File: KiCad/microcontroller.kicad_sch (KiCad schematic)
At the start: 48 parts, among them J4 Debugger, J5 STM32F051C6_male_header, SW1 Reset switch, SW2 switch, SW3 switch, SW4 switch, U7 24LC256

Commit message: Significant schematic changes
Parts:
- removed J5: STM32F051C6_male_header, symbol EEE3088F_CKR:STM32F051C6_male_header
- removed TP?: STM32 BOOT0, footprint:Testpoint_2.54mm, symbol Connector:TestPoint
- added J4: STM32F051C6_testpoints, symbol EEE3088F_CKR:STM32F051C6_testpoints
- added JP1, JP2, JP3, JP4, JP5, JP6: Jumper_2_Bridged, symbol Jumper:Jumper_2_Bridged
- added R48, R49, R50, R51, R57: 0, footprint:R0603, symbol Device:R
- renumbered J4 to J5, R52 to R34, R53 to R35, R30 to R36, R31 to R37, R32 to R38, R33 to R39, R34 to R40, R36 to R41, R37 to R42, R40 to R43, R41 to R44, R42 to R45, R43 to R46, R56 to R47, R61 to R60, R62 to R61, R63 to R62, R64 to R63
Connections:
- net INT_1 is gone; now on net INT: R?.1
- net uc29 is gone; now on net SW3: J3.29 (PA8_)
- net +3V3: now also J4.1 (_VBAT), J4.24 (_VDD), J4.48 (VDD_), J4.9 (_VDDA)
- net BOOT0: now also J4.44 (BOOT0_)
- net GND: now also J4.23 (_VSS), J4.47 (VSS_), J4.8 (_VSSA)
- net INT: now also J4.25 (PB12_)
- net LED1: now also J4.15 (_PA5)
- net LED2: now also J4.16 (_PA6)
- net Lght_P: now also J4.40 (PB4_)
- net NSRT: now also J4.7 (_NSRT)
- net POT: now also JP6.1 (A); no longer J3.19 (_PB1)
- net POT_P: now also J4.20 (_PB2)
- net Rx: now also J4.43 (PB7_)
- net SCL_1: now also JP1.1 (A); no longer J3.21 (_PB10), R?.1
- net SCL_2: now also JP3.1 (A); no longer J3.45 (PB8_), R?.1
- net SDA_1: now also JP2.1 (A); no longer J3.22 (_PB11), R?.1
- net SDA_2: now also JP4.1 (A); no longer J3.46 (PB9_), R?.1
- net SW1: now also J3.27 (PB14_), J4.27 (PB14_); no longer J3.26 (PB13_)
- net SW2: now also J3.28 (PB15_), J4.28 (PB15_); no longer J3.27 (PB14_)
- net SW3: now also J4.29 (PA8_); no longer J3.28 (PB15_)
- net SWCLK: now also J4.37 (PA14_)
- net SWDIO: now also J4.34 (PA13_)
- net THM: now also JP5.1 (A); no longer J3.18 (_PB0)
- net THM_P: now also J4.39 (PB3_)
- net TeHu_P: now also J4.41 (PB5_)
- net Tx: now also J4.42 (PB6_)
- net uc10: now also J4.10 (_PA0)
- net uc11: now also J4.11 (_PA1)
- net uc12: now also J4.12 (_PA2)
- net uc13: now also J4.13 (_PA3)
- net uc14: now also J4.14 (_PA4)
- net uc17: now also J4.17 (_PA7)
- net uc2: now also J4.2 (_PC13)
- net uc3: now also J4.3 (_PC14)
- net uc30: now also J4.30 (PA9_)
- net uc31: now also J4.31 (PA10_)
- net uc32: now also J4.32 (PA11_)
- net uc33: now also J4.33 (PA12_)
- net uc35: now also J4.35 (PA6_)
- net uc36: now also J4.36 (PF7_)
- net uc38: now also J4.38 (PA15_)
- net uc4: now also J4.4 (_PC15)
- net uc5: now also J4.5 (_PF0)
- net uc6: now also J4.6 (_PF1)
- new net Debugger_Potentiometer_signal: J3.19 (_PB1), J4.19 (_PB1), JP6.2 (B)
- new net Debugger_SCL: R48.2, R50.2
- new net Debugger_SDA: R49.2, R51.2
- new net Debugger_Thermistor_signal: J3.18 (_PB0), J4.18 (_PB0), JP5.2 (B)
- new net Plg_Dtct: J3.26 (PB13_), J4.26 (PB13_), R57.2
- new net Plug_Detect: R57.1
- new net SCL_1_uc: J3.21 (_PB10), J4.21 (_PB10), JP1.2 (B), R48.1, R?.1
- new net SCL_2_uc: J3.45 (PB8_), J4.45 (PB8_), JP3.2 (B), R50.1, R?.1
- new net SDA_1_uc: J3.22 (_PB11), J4.22 (_PB11), JP2.2 (B), R49.1, R?.1
- new net SDA_2_uc: J3.46 (PB9_), J4.46 (PB9_), JP4.2 (B), R51.1, R?.1
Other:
- note added: "Plug detect"
- note added: "Sensor data debugger links and jumpers"
- moved on the sheet: D4, D5, R34, R35, R36, R37, R38, R39, R40, R41, R42, R43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

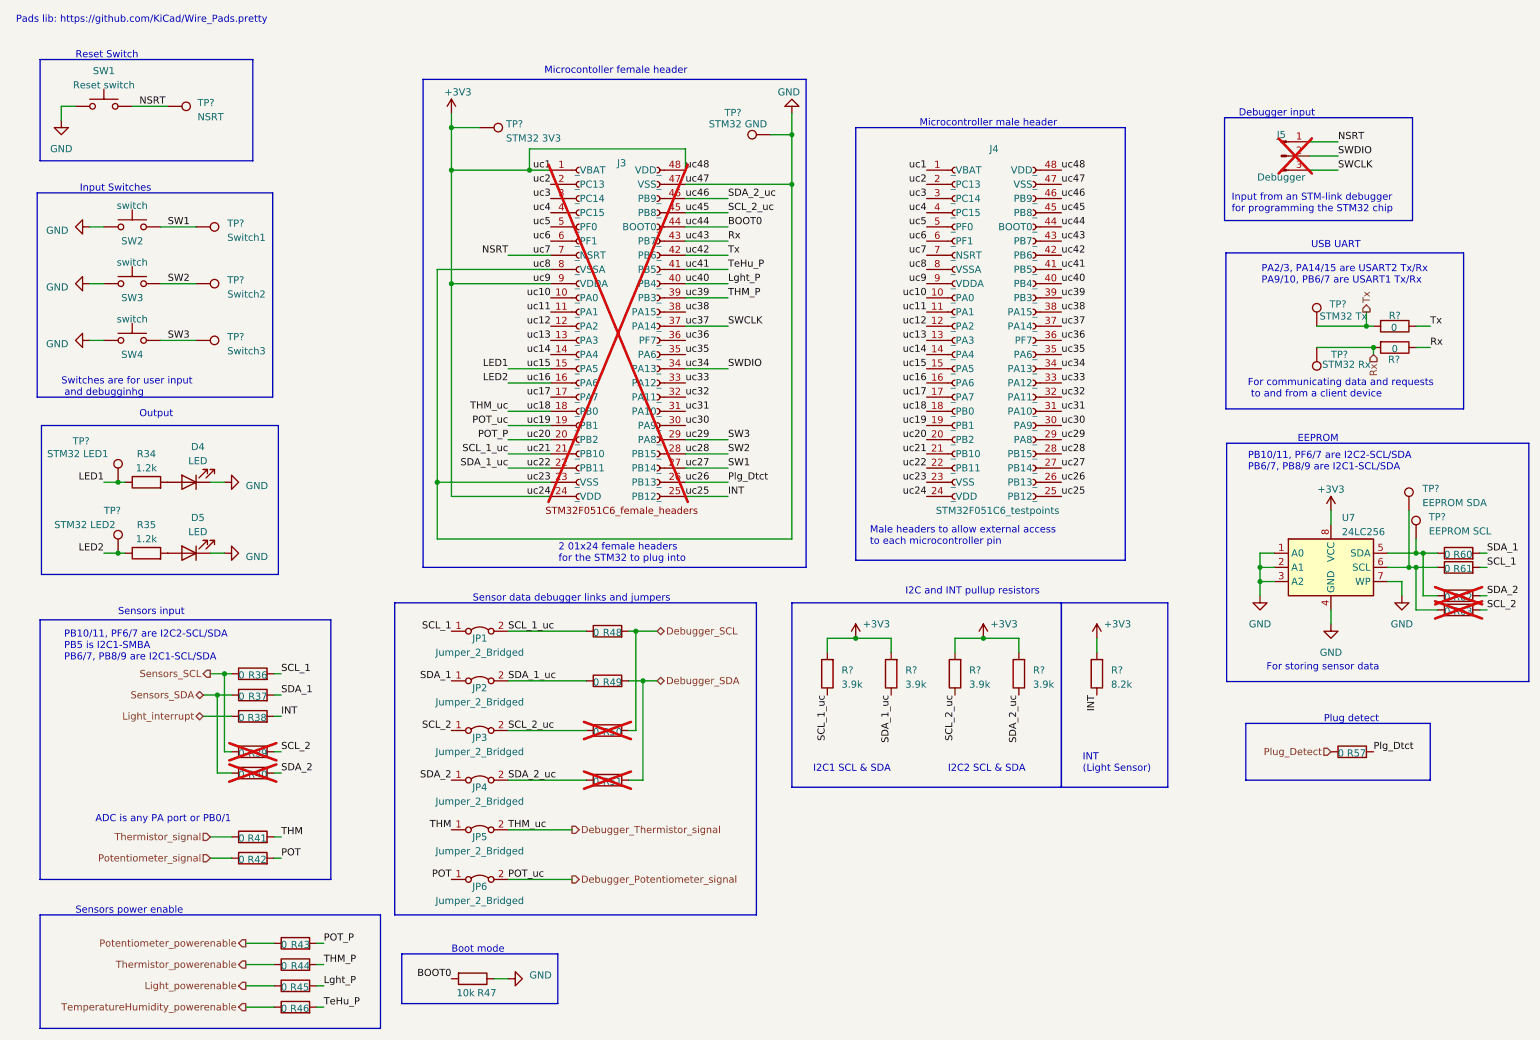
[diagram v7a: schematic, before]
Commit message: Corrected all part numbers and small schematic changes
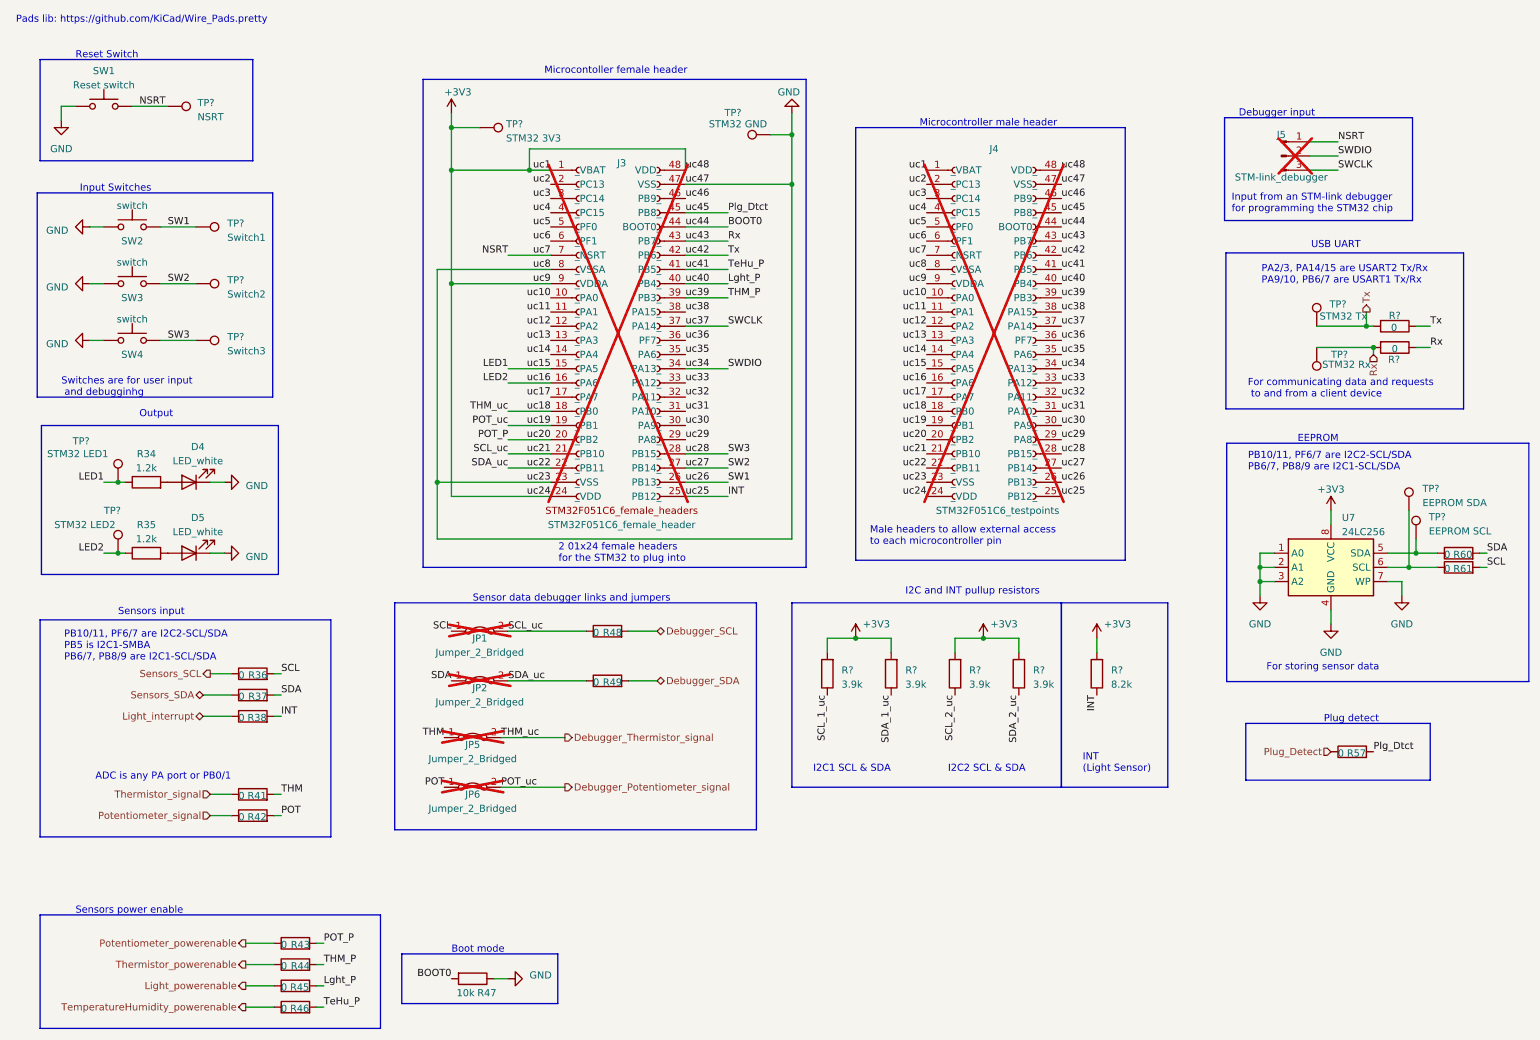
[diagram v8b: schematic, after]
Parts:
- removed JP3, JP4: Jumper_2_Bridged, symbol Jumper:Jumper_2_Bridged
- removed R39, R40, R50, R51, R62, R63: 0, footprint:R0603, symbol Device:R
- D4, D5: value LED -> LED_white; JLC code C2286 -> C34499; Part name LED_0603 -> C34499; cost per unit 0,0054 -> 0.0157
- J3: value ~ -> STM32F051C6_female_header; JLC code C2883741 -> (none); Part name X6511FV-24-C85D32 -> (none)
- J4, JP1, JP2, JP5, JP6: Extended Part Cost (none) -> 0; cost per unit (none) -> 0; now not fitted
- J5: value Debugger -> STM-link_debugger; JLC code C2886705 -> (none); Part name CS-1165SDIG-1*3 -> (none)
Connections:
- net Plg_Dtct: now also J3.45 (PB8_), J4.45 (PB8_); no longer J3.26 (PB13_), J4.26 (PB13_)
- net SCL_1_uc: no longer J3.21 (_PB10), J4.21 (_PB10), JP1.2 (B), R48.1
- net SCL_2_uc: no longer J3.45 (PB8_), J4.45 (PB8_)
- net SDA_1_uc: no longer J3.22 (_PB11), J4.22 (_PB11), JP2.2 (B), R49.1
- net SDA_2_uc: no longer J3.46 (PB9_), J4.46 (PB9_)
- net SW1: now also J3.26 (PB13_), J4.26 (PB13_); no longer J3.27 (PB14_), J4.27 (PB14_)
- net SW2: now also J3.27 (PB14_), J4.27 (PB14_); no longer J3.28 (PB15_), J4.28 (PB15_)
- net SW3: now also J3.28 (PB15_), J4.28 (PB15_); no longer J3.29 (PA8_), J4.29 (PA8_)
- net SCL_1 renamed SCL
- net SDA_1 renamed SDA
- new net SCL_uc: J3.21 (_PB10), J4.21 (_PB10), JP1.2 (B), R48.1
- new net SDA_uc: J3.22 (_PB11), J4.22 (_PB11), JP2.2 (B), R49.1
- new net uc29: J3.29 (PA8_), J4.29 (PA8_)
- new net uc46: J3.46 (PB9_), J4.46 (PB9_)
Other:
- moved on the sheet: R41, R42
